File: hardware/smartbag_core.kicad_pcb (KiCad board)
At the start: 4 copper layers, 196 x 20 mm, 26 parts, among them J1 FFC optics, 10 way, J2 LiPo 3.7V 2000mAh, J3 Qi RX coil, J4 FFC FSR matrix, 24 way, J5 SWD debug, U1 SoC+NPU BLE 5.4, U2 mmWave 60GHz TRX, U3 PMIC buck-boost, U4 6-axis IMU, U5 Hall, zip, Y1 32 MHz

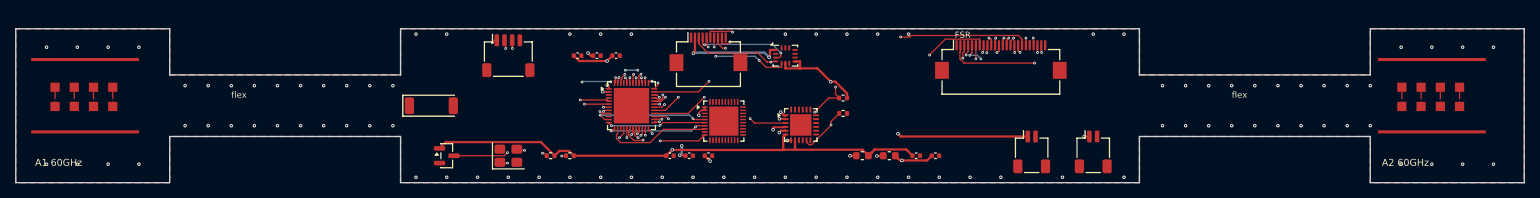
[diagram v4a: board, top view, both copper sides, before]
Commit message: Rebuild the board around parts you can actually buy
The board was drawn from component classes with invented pinouts. It said
so, and it was still unbuildable. Every IC is now a real part whose pinout
comes from its own datasheet, and tools/bom_report.py measures each
footprint against the datasheet's package on every run: 18 of 18 agree.

Finding the real parts changed the architecture three times, and each
change had already been asked for by something else in this repo:

- rf/feed_loss.py priced a central 60 GHz transceiver's feed at 8.2 dB one
  way. The Acconeer A121's datasheet says the antenna is inside the package
  and "it is not possible to connect trace antenna" — so there are now TWO
  sensors, one on each end island, and no 60 GHz copper on the board at
  all. ANT_A1 and ANT_A2 are gone.
- thermal/budget.py asked for charge current to be a function of cell
  temperature. RT1 is a 10k NTC into an nPM1300, which does JEITA charging
  in hardware.
- firmware/test_sb_fsr.c measured both scan modes the old board could run:
  phantom taxels at 39% of a real press, or real ones 83% light. The rows
  now land on six transimpedance amplifiers and the columns on a 16:1
  multiplexer.

And one thing the parts took away: no BLE SoC in a QFN has an NPU and a
camera interface. The processor is an nRF54L15, a 128 MHz Cortex-M33, and
recognition has to run on it. Survivable only because the firmware already
waits 2 s for an object to settle.

91 parts, four layers, routed: 1683 tracks, 393 vias, 0 DRC violations, 0
footprint errors, schematic parity clean, 3 unconnected pads of 462. In1.Cu
carries zero tracks and stays a solid ground reference.

New machinery, each written because something went wrong without it:

- place.py — the floorplan is a hint; 91 hand-typed coordinates collided in
  28 places. It also knows nothing may sit on a flex tail, after a pass put
  a 24-way connector out over one and off the board edge.
- stitch.py — routing cuts the top pour into isla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
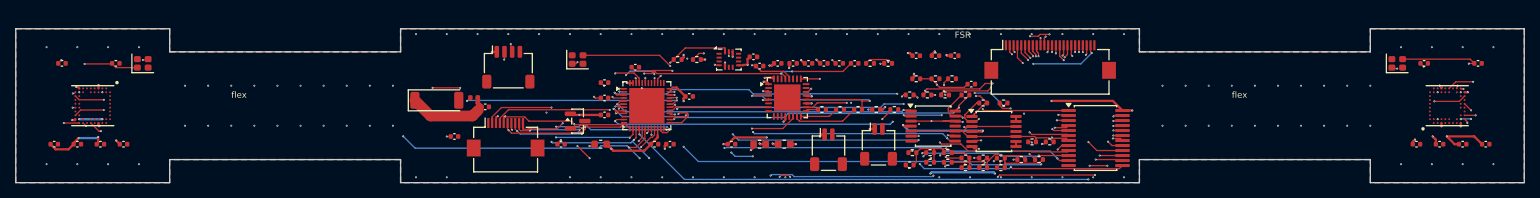
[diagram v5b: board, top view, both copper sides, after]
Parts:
- added C11: 0.3p C0G, Capacitor_SMD:C_0402_1005Metric, F.Cu at (173.0, 148.2)
- added C20: 1u X5R, Capacitor_SMD:C_0402_1005Metric, F.Cu at (117.0, 153.0)
- added C21: 1u X5R, Capacitor_SMD:C_0402_1005Metric, F.Cu at (120.0, 153.0)
- added C22: 1u X5R, Capacitor_SMD:C_0402_1005Metric, F.Cu at (123.0, 153.0)
- added C23: 1u X5R, Capacitor_SMD:C_0402_1005Metric, F.Cu at (126.0, 153.0)
- added C24: 8p NP0, Capacitor_SMD:C_0402_1005Metric, F.Cu at (125.0, 142.5)
- added C25: 8p NP0, Capacitor_SMD:C_0402_1005Metric, F.Cu at (118.0, 142.5)
- added C30: 1u X5R, Capacitor_SMD:C_0402_1005Metric, F.Cu at (303.0, 153.0)
- added C31: 1u X5R, Capacitor_SMD:C_0402_1005Metric, F.Cu at (300.0, 153.0)
- added C32: 1u X5R, Capacitor_SMD:C_0402_1005Metric, F.Cu at (297.0, 153.0)
- added C33: 1u X5R, Capacitor_SMD:C_0402_1005Metric, F.Cu at (294.0, 153.0)
- added C34: 8p NP0, Capacitor_SMD:C_0402_1005Metric, F.Cu at (295.0, 142.5)
- added C35: 8p NP0, Capacitor_SMD:C_0402_1005Metric, F.Cu at (302.0, 142.5)
- added C40: 10u X5R 6.3V, Capacitor_SMD:C_0402_1005Metric, F.Cu at (208.7, 142.8)
- added C41: 10u X5R 6.3V, Capacitor_SMD:C_0402_1005Metric, F.Cu at (211.0, 142.5)
- added C42: 10u X5R 6.3V, Capacitor_SMD:C_0402_1005Metric, F.Cu at (213.0, 142.5)
- added C43: 1u X5R, Capacitor_SMD:C_0402_1005Metric, F.Cu at (215.0, 142.5)
- added C44: 1u X5R, Capacitor_SMD:C_0402_1005Metric, F.Cu at (217.0, 142.5)
- added C45: 1u X5R, Capacitor_SMD:C_0402_1005Metric, F.Cu at (219.0, 142.5)
- added C46: 1u X5R, Capacitor_SMD:C_0402_1005Metric, F.Cu at (221.0, 142.5)
- added C50: 100n X7R, Capacitor_SMD:C_0402_1005Metric, F.Cu at (207.8, 141.7)
- added C51: 100n X7R, Capacitor_SMD:C_0402_1005Metric, F.Cu at (205.0, 153.0)
- added C52: 100n X7R, Capacitor_SMD:C_0402_1005Metric, F.Cu at (182.8, 153.0)
- added C60: 1u X5R, Capacitor_SMD:C_0402_1005Metric, F.Cu at (236.2, 145.2)
- added C61: 100n X7R, Capacitor_SMD:C_0402_1005Metric, F.Cu at (229.0, 141.5)
- added C62: 100n X7R, Capacitor_SMD:C_0402_1005Metric, F.Cu at (231.5, 141.5)
- added C63: 100n X7R, Capacitor_SMD:C_0402_1005Metric, F.Cu at (234.0, 141.5)
- added L3: 2.2u 1.2A, Inductor_SMD:L_0603_1608Metric, F.Cu at (208.7, 153.0)
- added L4: 2.2u 1.2A, Inductor_SMD:L_0603_1608Metric, F.Cu at (211.8, 153.0)
- added R10: 6.8k 1%, Resistor_SMD:R_0402_1005Metric, F.Cu at (229.0, 144.5)
- added R11: 1.2k 1%, Resistor_SMD:R_0402_1005Metric, F.Cu at (231.5, 144.5)
- added R12: 0R, Resistor_SMD:R_0402_1005Metric, F.Cu at (233.7, 144.5)
- added R40: 8.2k 1%, Resistor_SMD:R_0402_1005Metric, F.Cu at (228.2, 146.6)
- added R41: 8.2k 1%, Resistor_SMD:R_0402_1005Metric, F.Cu at (230.4, 146.6)
- added R42: 8.2k 1%, Resistor_SMD:R_0402_1005Metric, F.Cu at (232.8, 146.6)
- added R43: 8.2k 1%, Resistor_SMD:R_0402_1005Metric, F.Cu at (235.4, 146.6)
- added R44: 8.2k 1%, Resistor_SMD:R_0402_1005Metric, F.Cu at (237.7, 147.7)
- added R45: 8.2k 1%, Resistor_SMD:R_0402_1005Metric, F.Cu at (240.3, 147.7)
- added R5: 10k 1%, Resistor_SMD:R_0402_1005Metric, F.Cu at (223.8, 148.5)
- added R6: 1k 1%, Resistor_SMD:R_0402_1005Metric, F.Cu at (226.2, 148.5)
- added R60: 100k 1%, Resistor_SMD:R_0402_1005Metric, F.Cu at (228.2, 155.7)
- added R61: 100k 1%, Resistor_SMD:R_0402_1005Metric, F.Cu at (230.8, 155.3)
- added R62: 100k 1%, Resistor_SMD:R_0402_1005Metric, F.Cu at (233.1, 155.3)
- added R63: 100k 1%, Resistor_SMD:R_0402_1005Metric, F.Cu at (235.4, 156.1)
- added R64: 100k 1%, Resistor_SMD:R_0402_1005Metric, F.Cu at (237.7, 156.1)
- added R65: 100k 1%, Resistor_SMD:R_0402_1005Metric, F.Cu at (240.0, 156.1)
- added R66: 100k 1%, Resistor_SMD:R_0402_1005Metric, F.Cu at (242.7, 155.0)
- added R67: 100k 1%, Resistor_SMD:R_0402_1005Metric, F.Cu at (244.9, 155.0)
- added R68: 100k 1%, Resistor_SMD:R_0402_1005Metric, F.Cu at (228.5, 154.1)
- added R69: 100k 1%, Resistor_SMD:R_0402_1005Metric, F.Cu at (230.8, 154.1)
- added R7: 4.7k 1%, Resistor_SMD:R_0402_1005Metric, F.Cu at (198.0, 142.0)
- added R70: 100k 1%, Resistor_SMD:R_0402_1005Metric, F.Cu at (233.1, 154.1)
- added R71: 100k 1%, Resistor_SMD:R_0402_1005Metric, F.Cu at (235.4, 154.8)
- added R72: 100k 1%, Resistor_SMD:R_0402_1005Metric, F.Cu at (237.7, 154.8)
- added R73: 100k 1%, Resistor_SMD:R_0402_1005Metric, F.Cu at (240.0, 154.8)
- added R74: 100k 1%, Resistor_SMD:R_0402_1005Metric, F.Cu at (244.1, 152.7)
- added R75: 100k 1%, Resistor_SMD:R_0402_1005Metric, F.Cu at (246.3, 152.7)
- added R8: 4.7k 1%, Resistor_SMD:R_0402_1005Metric, F.Cu at (200.5, 142.0)
- added RT1: 10k NTC B3380, Resistor_SMD:R_0402_1005Metric, F.Cu at (223.0, 142.5)
- added U6: Acconeer A121, SmartBag:Acconeer_A121_fcCSP50, F.Cu at (298.0, 148.0)
- added U7: CD74HC4067SM96, Package_SO:SSOP-24_5.3x8.2mm_P0.65mm, F.Cu at (252.3, 152.2)
- added U8: TLV9064IPWR, Package_SO:TSSOP-14_4.4x5mm_P0.65mm, F.Cu at (231.2, 150.7)
- added U9: TLV9064IPWR, Package_SO:TSSOP-14_4.4x5mm_P0.65mm, F.Cu at (239.1, 151.3)
- added Y2: 24 MHz, Crystal:Crystal_SMD_2016-4Pin_2.0x1.6mm, F.Cu at (128.5, 142.5)
- added Y3: 24 MHz, Crystal:Crystal_SMD_2016-4Pin_2.0x1.6mm, F.Cu at (291.5, 142.5)
- AE1: value 2.4 GHz chip antenna -> 2450AT43F0100E
- C1, C2: value 100n -> 2.2u X6T 2.5V
- C3: value 4u7 -> 10u X6S 6.3V
- C4: value 1u -> 100n X7R
- C5: value 100n -> 2.2n X7R
- C6: value 10u -> 1.5p NP0
- C7, C8: value 22u -> 100n X7R
- L1: value 2u2 -> 4.7u 120mA
- L2: value 1u0 -> 2.7n; footprint Inductor_SMD:L_0603_1608Metric -> Inductor_SMD:L_0402_1005Metric
- R1, R2, R3: value 10k -> 10k 1%
- R4: value 100k -> 1M 1%
- U1: value SoC+NPU BLE 5.4 -> nRF54L15-QFAA-R
- U2: value mmWave 60GHz TRX -> Acconeer A121; footprint Package_DFN_QFN:QFN-40-1EP_5x5mm_P0.4mm_EP3.8x3.8mm -> SmartBag:Acconeer_A121_fcCSP50
- U3: value PMIC buck-boost -> nPM1300-QEAA-R7; footprint Package_DFN_QFN:QFN-24-1EP_4x4mm_P0.5mm_EP2.8x2.8mm -> Package_DFN_QFN:QFN-32-1EP_5x5mm_P0.5mm_EP3.45x3.45mm
- U4: value 6-axis IMU -> BMI270
- U5: value Hall, zip -> DRV5032FBDBZR
- Y1: value 32 MHz -> 32 MHz Cl=8pF; footprint Crystal:Crystal_SMD_3225-4Pin_3.2x2.5mm -> Crystal:Crystal_SMD_2016-4Pin_2.0x1.6mm
- moved U2 82.0 mm to (122.0, 148.0), turned to -90 degrees
- moved L2 54.5 mm to (171.6, 146.9)
- moved R1 45.5 mm to (225.3, 142.5)
- moved J2 34.4 mm to (217.6, 153.7)
- moved C7 34.0 mm to (195.0, 153.0)
- moved L1 34.0 mm to (188.0, 153.0)
- moved R2 33.3 mm to (216.8, 148.5)
- moved C6 33.1 mm to (169.0, 152.0)
- moved C8 32.9 mm to (199.5, 146.8)
- moved J1 28.6 mm to (175.7, 152.1)
- moved J3 19.9 mm to (224.1, 153.0)
- moved U5 17.6 mm to (185.0, 150.0)
- moved Y1 15.4 mm to (185.0, 142.0)
- moved C3 13.5 mm to (197.0, 153.0)
- moved C5 13.5 mm to (192.5, 143.0)
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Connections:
- C1 pad 1: VDD_1V8 -> DECA
- C2 pad 1: VDD_3V3 -> DECD
- C3 pad 1: VDD_1V8 -> VDD_3V3
- C5 pad 1: VDD_1V8 -> DECRF
- C6 pad 1: VBAT -> ANT_FEED
- C8 pad 1: VDD_1V8 -> VDD_3V3
- J1 pad 10: GND -> CAM_RESET
- J1 pad 2: VDD_3V3 -> VDD_CAM
- J1 pad 5: CAM_CLK -> SPI_SCK
- J1 pad 6: CAM_DATA -> SPI_MOSI
- J1 pad 7: CAM_PWDN -> SPI_MISO
- J1 pad 8: LED_PWM -> CS_CAM
- J1 pad 9: TOF_INT -> CAM_PWDN
- J5 pad 1: SWDIO -> VDD_3V3
- J5 pad 2: SWCLK -> SWDCLK
- J5 pad 3: nRESET -> SWDIO
- L1 pad 1: SW1 -> DCC
- L2 pad 1: SW2 -> ANT_FEED
- L2 pad 2: VDD_1V8 -> BLE_ANT
- R1 pad 1: nRESET -> VSYS
- R1 pad 2: VDD_3V3 -> NTC
- R2 pad 1: I2C_SDA -> VSET1
- R2 pad 2: VDD_3V3 -> GND
- R3 pad 1: I2C_SCL -> VSET2
- R3 pad 2: VDD_3V3 -> GND
- R4 pad 1: VBAT_SNS -> SHPHLD
- R4 pad 2: GND -> VSYS
- U1 pad 1: VDD_1V8 -> CAM_PWDN
- U1 pad 10: BLE_ANT -> VDD_3V3
- U1 pad 11: SPI_SCK -> MUX_S3
- U1 pad 12: SPI_MOSI -> SPI_SCK
- U1 pad 13: SPI_MISO -> SPI_MOSI
- U1 pad 14: SPI_CS -> CS_RADAR_L
- U1 pad 15: RADAR_IRQ -> SPI_MISO
- U1 pad 16: I2C_SDA -> CS_RADAR_R
- U1 pad 17: I2C_SCL -> CS_CAM
- U1 pad 18: IMU_INT -> RADAR_EN
- U1 pad 19: HALL -> RADAR_IRQ_L
- U1 pad 2: VDD_3V3 -> CAM_RESET
- U1 pad 20: TOF_INT -> RADAR_IRQ_R
- U1 pad 21: CAM_CLK -> MUX_EN_N
- U1 pad 22: CAM_DATA -> VDD_3V3
- U1 pad 23: CAM_PWDN -> I2C_SDA
- U1 pad 24: LED_PWM -> I2C_SCL
- U1 pad 25: VBAT_SNS -> SWDIO
- U1 pad 26: PMIC_EN -> SWDCLK
- U1 pad 27: FSR_C0 -> IMU_INT1
- U1 pad 28: FSR_C1 -> HALL_OUT
- U1 pad 29: FSR_C2 -> PMIC_IRQ
- U1 pad 3: GND -> MUX_S0
- U1 pad 30: FSR_C3 -> NRESET
- U1 pad 31: FSR_C4 -> ANT_FEED
- U1 pad 32: FSR_C5 -> GND
- U1 pad 33: FSR_C6 -> DECRF
- U1 pad 34: FSR_C7 -> XTAL32M_1
- U1 pad 35: FSR_C8 -> XTAL32M_2
- U1 pad 36: FSR_C9 -> VDD_3V3
- U1 pad 37: FSR_C10 -> unconnected-(U1-P1.09-Pad37)
- U1 pad 38: FSR_C11 -> unconnected-(U1-P1.10-Pad38)
- U1 pad 39: FSR_C12 -> ADC4
- U1 pad 4: GND -> MUX_S1
- U1 pad 40: FSR_C13 -> ADC5
- U1 pad 41: FSR_C14 -> unconnected-(U1-P1.13/AIN6-Pad41)
- U1 pad 42: FSR_C15 -> unconnected-(U1-P1.14/AIN7-Pad42)
- U1 pad 43: FSR_R0 -> DECA
- U1 pad 44: FSR_R1 -> GND
- U1 pad 45: FSR_R2 -> DECD
- U1 pad 46: FSR_R3 -> DCC
- U1 pad 47: FSR_R4 -> VDD_3V3
- U1 pad 48: FSR_R5 -> VDD_3V3
- U1 pad 5: XTAL_I -> ADC0
- U1 pad 6: XTAL_O -> ADC1
- U1 pad 7: nRESET -> ADC2
- U1 pad 8: SWDIO -> ADC3
- U1 pad 9: SWCLK -> MUX_S2
- U3 pad 1: VBAT -> VDD_1V8
- U3 pad 11: VBAT_SNS -> GND
- U3 pad 12: GND -> VDD_3V3
- U3 pad 13: GND -> I2C_SDA
- U3 pad 14: GND -> I2C_SCL
- U3 pad 15: GND -> SHPHLD
- U3 pad 16: GND -> VSET2
- U3 pad 17: GND -> VSET1
- U3 pad 18: GND -> NTC
- U3 pad 19: GND -> VBAT
- U3 pad 2: VQI -> GND
- U3 pad 20: GND -> VSYS
- U3 pad 21: GND -> VQI
- U3 pad 22: GND -> VBUSOUT
- U3 pad 25: GND -> LED0
- U3 pad 3: PMIC_EN -> SW1
- U3 pad 4: SW1 -> VSYS
- U3 pad 6: VDD_3V3 -> GND
- U3 pad 7: VDD_1V8 -> PMIC_IRQ
- U3 pad 8: VDD_3V3 -> GND
- U4 pad 1: VDD_3V3 -> GND
- U4 pad 12: GND -> VDD_3V3
- U4 pad 13: GND -> I2C_SCL
- U4 pad 14: GND -> I2C_SDA
- U4 pad 3: I2C_SDA -> GND
- U4 pad 4: I2C_SCL -> IMU_INT1
- U4 pad 5: IMU_INT -> VDD_3V3
- U4 pad 6: VDD_3V3 -> GND
- U4 pad 9: GND -> unconnected-(U4-INT2-Pad9)
- U5 pad 2: GND -> HALL_OUT
- U5 pad 3: HALL -> GND
- Y1 pad 1: XTAL_I -> XTAL32M_1
- Y1 pad 3: XTAL_O -> XTAL32M_2
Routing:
- net SPI_MOSI: track 12.8 -> 215.9 mm, vias 2 -> 6
- net RADAR_EN: track 0.00 -> 199.1 mm, vias 0 -> 9
- net SPI_SCK: track 15.2 -> 205.5 mm, vias 2 -> 6
- net SPI_MISO: track 13.0 -> 197.8 mm, vias 2 -> 12
- net VDD_3V3: track 136.5 -> 311.1 mm, vias 6 -> 33
- net VDD_1V8: track 82.5 -> 241.1 mm, vias 7 -> 19
- net RADAR_IRQ_R: track 0.00 -> 121.0 mm, vias 0 -> 6
- net CS_RADAR_R: track 0.00 -> 116.3 mm, vias 0 -> 4
- net RADAR_IRQ_L: track 0.00 -> 92.3 mm, vias 0 -> 2
- net VREF: track 0.00 -> 82.5 mm, vias 0 -> 5
- net CS_RADAR_L: track 0.00 -> 82.2 mm, vias 0 -> 3
- net MUX_S1: track 0.00 -> 74.7 mm, vias 0 -> 3
- net MUX_S3: track 0.00 -> 72.4 mm, vias 0 -> 4
- net MUX_S2: track 0.00 -> 71.5 mm, vias 0 -> 4
- net MUX_EN_N: track 0.00 -> 68.3 mm, vias 0 -> 4
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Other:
- outline, holes or cut-outs redrawn
- board text added: "U2/U6 A121: 60 GHz radar, antenna in package"
- board text added: "U2/U6 need solid ground under the whole package (A121 ds 5.4)"
- board text added: "no 60 GHz copper on this board: the antennas are inside the A121"
- board text removed: "A1 60GHz"
- board text removed: "A1/A2 2x4 patch array, lambda0/2 pitch"
- board text removed: "A1/A2 islands: 0.25 mm dielectric under the patches, NOT 0.6"
- board text removed: "A2 60GHz"
- board text removed: "full-wave sim: 0.25 mm -> -27 dB at 59.9 GHz; 0.6 mm -> -2.5 dB"

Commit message: Choose the camera, cost the inference, and let the antenna datasheet win
Three things were still open. Each turned out to be answerable rather
than a matter of taste, and two of them found errors.

CAMERA. The SoC has no camera interface, so the module has to be SPI:
Arducam Mega 3MP NoIR (B0435), six wires, no IR-cut filter, 3.3 V,
56-136 mA. J1 was carrying I2C, a power-down and a reset that this part
does not have; those three ways now carry the thing the board was
actually missing — a way to switch the illuminators. thermal/budget.py
had been costing them at 0.6 W for a hundredth of a second since before
there was anything to switch them with. Q1 is that switch, with a gate
pull-down so they are dark while the processor is in reset.

The camera also freed XL1/XL2, which are now a 32.768 kHz crystal. The
app puts an age on every position it reports; the internal RC is
+/-500 ppm, which is 43 seconds a day, and a claim about a clock deserves
a clock.

NPU. ml/inference_budget.py counts the MACs by running a tensor through
the model in classify.py with hooks, reads the camera's SPI ceiling from
the chosen part and the deadlines from firmware/smartbag.h. 6.99 M MACs
a frame, 110-191 ms end to end against a 2000 ms settle window: it fits
by 10.5x at the pessimistic bound. The NPU was never needed at this model
size. The same arithmetic sets a limit nobody had written down: 320x240
RGB565 is 461 ms for a three-frame burst against a 400 ms capture
timeout, so the camera must be configured low.

ANTENNA. Reading the Johanson datasheet found three errors:
- terminal 2 was tied to GROUND and the terminal table says NC. It is a
  mechanical anchor; grounding it loads the radiator and no match
  recovers from that. It had been there since the first netlist, because
  a pad tied to ground is unremarkable in every check this project runs.
- the body was recorded as 3.2 x 1.6 mm and is 6.0 x 2.0.
- the ground plane ran straight under it. The datasheet calls for a
  7.0 x 2.2 m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
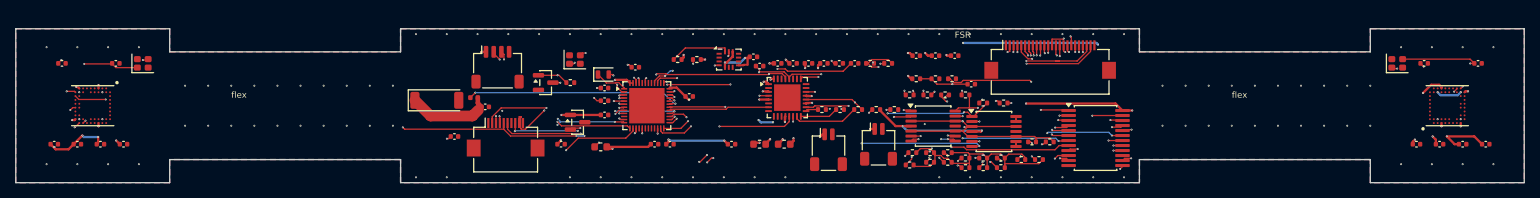
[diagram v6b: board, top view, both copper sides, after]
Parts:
- added Q1: SI2302CDS-T1-GE3, Package_TO_SOT_SMD:SOT-23, F.Cu at (180.8, 145.0)
- added R13: 100k 1%, Resistor_SMD:R_0402_1005Metric, F.Cu at (184.1, 145.0)
- added Y4: 32.768 kHz Cl=9pF, Crystal:Crystal_SMD_2012-2Pin_2.0x1.2mm, F.Cu at (188.3, 143.9)
- moved J5 1.40 mm to (174.6, 143.0)
- moved C1 0.70 mm to (188.5, 145.7)
- moved C2 0.35 mm to (188.5, 147.3)
- moved L1 0.35 mm to (188.0, 153.3)
- moved Y1 0.35 mm to (184.7, 142.0)
- moved U5 0.15 mm to (185.0, 150.2)
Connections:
- AE1 pad 2: GND -> unconnected-(AE1-NC-Pad2)
- J1 pad 10: CAM_RESET -> GND
- J1 pad 3: I2C_SCL -> SPI_SCK
- J1 pad 4: I2C_SDA -> SPI_MOSI
- J1 pad 5: SPI_SCK -> SPI_MISO
- J1 pad 6: SPI_MOSI -> CS_CAM
- J1 pad 7: SPI_MISO -> GND
- J1 pad 8: CS_CAM -> VSYS
- J1 pad 9: CAM_PWDN -> IR_LED_K
- U1 pad 1: CAM_PWDN -> XTAL32K_1
- U1 pad 2: CAM_RESET -> XTAL32K_2
- U1 pad 37: unconnected-(U1-P1.09-Pad37) -> IR_LED_EN
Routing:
- net RADAR_EN: track 199.1 -> 0.00 mm, vias 9 -> 0
- net SPI_MOSI: track 215.9 -> 79.3 mm, vias 6 -> 3
- net SPI_MISO: track 197.8 -> 76.5 mm, vias 12 -> 5
- net RADAR_IRQ_R: track 121.0 -> 0.00 mm, vias 6 -> 0
- net CS_RADAR_R: track 116.3 -> 0.00 mm, vias 4 -> 1
- net SPI_SCK: track 205.5 -> 90.2 mm, vias 6 -> 5
- net RADAR_IRQ_L: track 92.3 -> 0.00 mm, vias 2 -> 0
- net MUX_EN_N: track 68.3 -> 0.00 mm, vias 4 -> 0
- net VSYS: track 42.9 -> 69.7 mm, vias 4 -> 9
- net CAM_PWDN: track 23.6 -> 0.00 mm, vias 3 -> 0
- net IR_LED_EN: track 0.00 -> 19.7 mm, vias 0 -> 2
- net I2C_SCL: track 61.1 -> 43.1 mm, vias 6 -> 4
- net CAM_RESET: track 16.1 -> 0.00 mm, vias 2 -> 0
- net IR_LED_K: track 0.00 -> 12.1 mm, vias 0 -> 2
- net FSR_C0: track 42.3 -> 54.0 mm
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
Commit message: The ToF sensor the firmware always assumed, and fiducials
Two production blockers, both of them things that were invisible to every
check this project runs.

THE TIME-OF-FLIGHT SENSOR. firmware/smartbag.h has declared
SB_EV_TOF_CROSSED since the first commit — the beam across the mouth
breaking is what arms the camera — dimensions.py has placed a sensor at
TOF_X = 48, and the films show it working. No schematic ever contained
one. The wake-up chain depended on an event no hardware could raise.

It is a VL53L1X (LGA-12, 4.9 x 2.5 mm, I2C, XSHUT and GPIO1), it lives on
the optics flex because it has to look across the opening, and J1 grew
from ten ways to twelve to carry its I2C, shutdown and interrupt. KiCad
ships the footprint, so nothing was hand-drawn.

tools/check.py now reads the firmware's event enum against the netlist and
asserts that every event has a net that could produce it. The check was
negative-tested: removing TOF_INT makes it fail with "SB_EV_TOF_CROSSED
needs TOF_INT".

FIDUCIALS. The board had none, which means no assembly house would quote
it — a placement machine finds the board by looking at fiducials, and this
one has two 50-ball BGAs at 0.5 mm pitch. Three global in an L, so the
machine can tell which way round the board is, plus one local beside each
A121, because at 0.5 mm pitch a reference 90 mm away across a flex strip
that has just been through reflow is not a reference.

They are in the NETLIST, not just on the board: placed board-only they
produce five "extra footprint" parity warnings forever. Getting them to
match took two more corrections, both of which were DRC being right — a
fiducial's pad has an EMPTY number because it is a camera target and not
a connection, so the symbol has no pins either; and the footprint carries
exclude_from_bom, so the symbol has to say in_bom no.

ERC 0, DRC 0 errors, schematic parity clean, 4 unconnected pads.

Co-Authored-By: Claude Opus 5 <noreply@anthropic.com>
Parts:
- added FID1: fiducial, Fiducial:Fiducial_1mm_Mask2mm, F.Cu at (118.0, 140.5)
- added FID2: fiducial, Fiducial:Fiducial_1mm_Mask2mm, F.Cu at (302.0, 140.5)
- added FID3: fiducial, Fiducial:Fiducial_1mm_Mask2mm, F.Cu at (118.0, 155.5)
- added FID4: fiducial, Fiducial:Fiducial_1mm_Mask2mm, F.Cu at (130.5, 154.5)
- added FID5: fiducial, Fiducial:Fiducial_1mm_Mask2mm, F.Cu at (289.5, 154.5)
- J1: value FFC optics, 10 way -> FFC optics, 12 way; footprint Connector_FFC-FPC:Hirose_FH12-10S-0.5SH_1x10-1MP_P0.50mm_Horizontal -> Connector_FFC-FPC:Hirose_FH12-12S-0.5SH_1x12-1MP_P0.50mm_Horizontal
- moved C6 0.70 mm to (168.3, 152.0)
- moved C52 0.35 mm to (183.2, 153.0)
- moved J1 0.35 mm to (176.0, 152.1)
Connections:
- J1 pad 10: GND -> TOF_INT
- J1 pad 7: GND -> I2C_SDA
- J1 pad 8: VSYS -> I2C_SCL
- J1 pad 9: IR_LED_K -> TOF_XSHUT
- U1 pad 38: unconnected-(U1-P1.10-Pad38) -> TOF_XSHUT
- U1 pad 42: unconnected-(U1-P1.14/AIN7-Pad42) -> TOF_INT
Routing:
- net RADAR_EN: track 0.00 -> 205.9 mm, vias 0 -> 4
- net SPI_MISO: track 76.5 -> 200.2 mm, vias 5 -> 8
- net CS_RADAR_R: track 0.00 -> 122.6 mm, vias 1 -> 4
- net SPI_MOSI: track 79.3 -> 200.6 mm, vias 3 -> 5
- net RADAR_IRQ_R: track 0.00 -> 113.1 mm, vias 0 -> 3
- net SPI_SCK: track 90.2 -> 199.4 mm, vias 5 -> 6
- net RADAR_IRQ_L: track 0.00 -> 82.2 mm, vias 0 -> 2
- net MUX_EN_N: track 0.00 -> 65.9 mm, vias 0 -> 4
- net I2C_SDA: track 36.2 -> 70.1 mm, vias 3 -> 6
- net TOF_XSHUT: track 0.00 -> 27.9 mm, vias 0 -> 2
- net I2C_SCL: track 43.1 -> 70.6 mm, vias 4 -> 6
- net TOF_INT: track 0.00 -> 22.4 mm, vias 0 -> 2
- net VSYS: track 69.7 -> 77.6 mm, vias 9 -> 7
- net VDD_CAM: track 53.7 -> 61.2 mm
- net ADC3: track 61.8 -> 54.7 mm, vias 4 -> 2
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
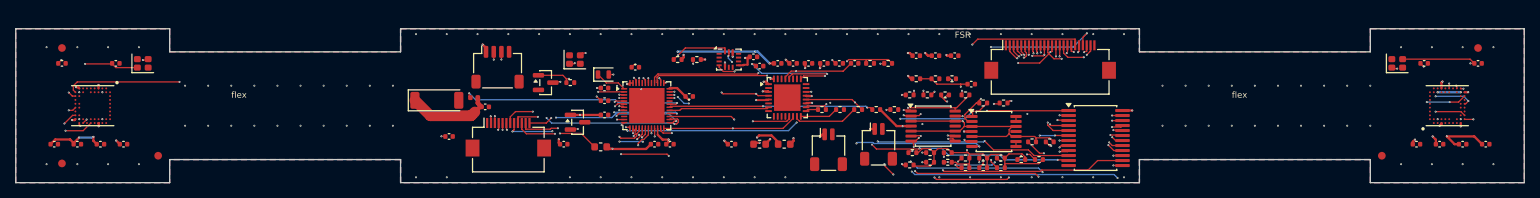
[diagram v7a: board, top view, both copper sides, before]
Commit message: finish.py: try the last few connections, with DRC as the judge
Freerouting recommends something it cannot do — "it is recommended to
stop it and finish the board manually" — and manually is fine, but a
person drawing four tracks and eyeballing them is exactly the step this
project avoids everywhere else.

So the candidates are drawn blind: seven shapes per unconnected pad
(straight and both L-bends, on the pad's own layer and through vias to
two others), each applied, each judged by a full DRC run, and kept only
if the board came out with fewer unconnected pads and no new violations.
Anything else is reverted. It cannot make the board worse.

On the four pads left on the insert board it reports that none of the
seven fits, which is the truthful answer: two VDD_3V3 pins on parts whose
neighbourhood is full, and two ground pour islands with nowhere to put a
via. They are named in the README rather than rounded away.

Two bugs in it, both caught by running it:
- it only looked for the pad on the FIRST line of a DRC pair, so it
  silently skipped half the work and reported the rest as done. DRC
  prints the two ends in whatever order it found them.
- it reverted by reloading the board from the file it had just written
  the failed candidate into. Three rejected tracks accumulated in the
  board and the tool reported the damage as its starting state. It now
  keeps a pristine copy on disk.

State across all three boards: insert 0 violations / 4 pads, optics 0 / 2,
taxels 0 / 0. ERC clean, schematic parity clean, 22 of 22 named parts fit
their footprints, 690 firmware assertions.

Co-Authored-By: Claude Opus 5 <noreply@anthropic.com>
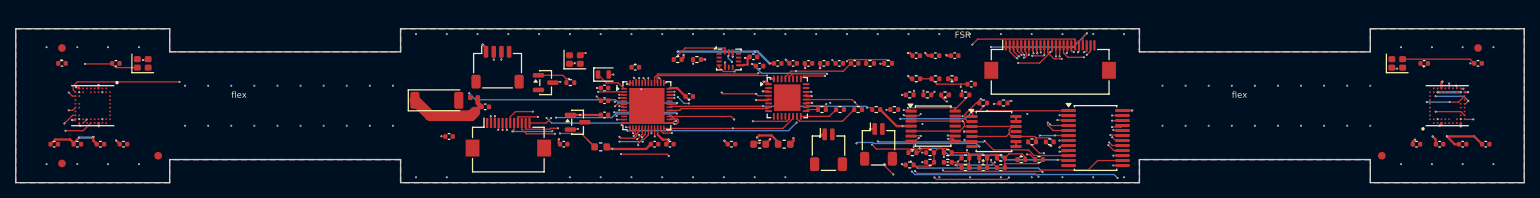
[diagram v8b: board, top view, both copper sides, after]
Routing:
- net DCC: track 18.8 -> 20.1 mm
